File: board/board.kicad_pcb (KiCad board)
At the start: 2 copper layers, 21 x 13 mm, 5 parts, among them J1 004_BASE-T_CT, J2 013_PoE_rectified

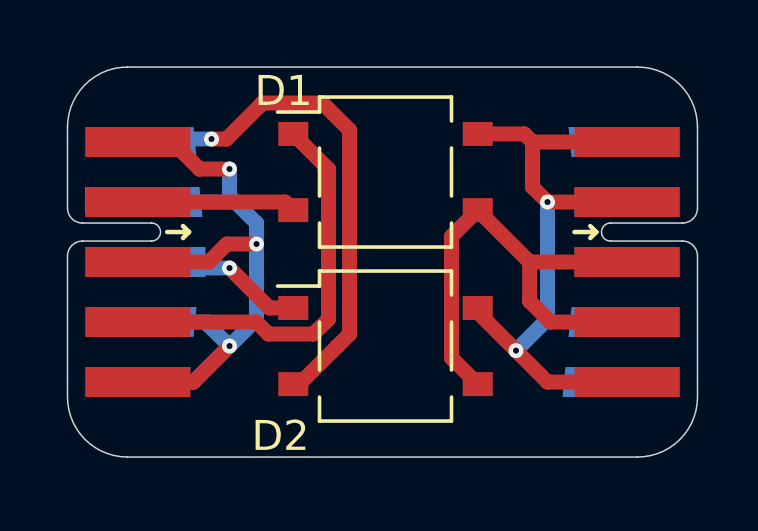
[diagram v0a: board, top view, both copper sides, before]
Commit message: updated to v1.0 of put_on_edge
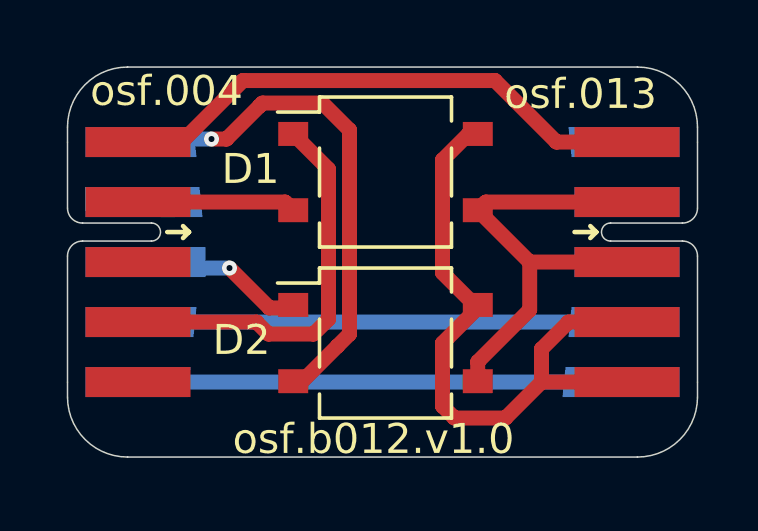
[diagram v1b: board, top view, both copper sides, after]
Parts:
- moved D2 0.10 mm to (150.6, 99.2)
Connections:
- D1 pad 4: GND -> /rectifier/PoE-
- D2 pad 4: GND -> /rectifier/PoE-
- J1 pad 1: Net-(J1-Pad1) -> GND
- J1 pad 10: Net-(J1-Pad1) -> Net-(J1-Pad10)
- J1 pad 3: Net-(J1-Pad1) -> (no net)
- J1 pad 5: Net-(J1-Pad1) -> (no net)
- J1 pad 7: Net-(J1-Pad1) -> (no net)
- J1 pad 9: Net-(J1-Pad1) -> Net-(J2-Pad9)
- J2 pad 10: (no net) -> Net-(J1-Pad10)
- J2 pad 2: GND -> /rectifier/48V
- J2 pad 4: /rectifier/48V -> /rectifier/PoE-
- J2 pad 5: GND -> /rectifier/PoE-
- J2 pad 9: (no net) -> Net-(J2-Pad9)
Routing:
- net Net-(J1-Pad1): track 28.3 -> 0.00 mm, vias 3 -> 0
- net /rectifier/PoE-: track 0.00 -> 21.8 mm
- net Net-(J2-Pad9): track 0.00 -> 16.2 mm
- net Net-(J1-Pad10): track 0.00 -> 16.2 mm
- net GND: track 21.4 -> 18.0 mm, vias 2 -> 0
- net /rectifier/48V: track 17.1 -> 15.6 mm
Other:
- board text added: "osf.004"
- board text added: "osf.013"
- board text added: "osf.b012.v1.0"
